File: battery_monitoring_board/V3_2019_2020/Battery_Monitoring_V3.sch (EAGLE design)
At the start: 82 parts, among them CON1 MOLEX_5566-2, CON2 SM03B-GHS-TB, CON3 SM03B-GHS-TB, J1 MKDS_5/2-6,352, J2 MKDS_5/2-6,352, J3 MKDS_5/2-6,352, J4 MKDS_5/2-6,352, J5 MKDS_5/2-6,352, J6 MKDS_5/2-6,352, J7 MKDS_5/2-6,352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

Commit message: battery_monitoring_board: moved V3 out into new folder
BOM and other exports still need to be finished
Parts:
- added D4: BZT52C10, Moira:BZT52C10
- added J10, J11: MKDS_5/2-6,352, Moira:MKDS_5/2-6,352
- added Q15: PSMN1R5-30BLE, Moira:PSMN1R5-30BLE
- added Q16: TCLD1000CT, Moira:TCLD1000CT
- added Q8: SI7145DP, Si7145DP:SI7145DP
- added R31, R32: 10k, adafruit:R-US_M1206
- added R33: 1k, adafruit:R-US_M1206
- added R34: 1k, adafruit:R-US_R0805
- added R35: 0.001Ohm, Moira:HCS3920FT1L00
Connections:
- new net BATT5GND: D4.A, J10.KL, Q15.S, R31.1, R32.1
- new net BATTERY5_IN: J10.KL1, Q8.S
- new net BATTERY_5: Q16.C2, Q8.D, R35.2, U1.IN+3
- new net MG4: D4.C, Q15.G, R32.2, R33.1
- new net MOTOR4: J11.KL, R35.1, U1.IN-3
- new net N$10: Q8.G, R31.2
- new net N$15: Q16.E, R33.2
- new net N$16: Q16.A, R34.2
- net +5V: now also R34.1
- net GND: now also J11.KL1, Q15.D
- net MOTOR2: no longer U1.IN-3
- net N$4: now also Q16.C1
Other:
- note added: "motor Gnd"
- moved on the sheet: CON1G$1, CON1G$2, JP1, JP2, JP3

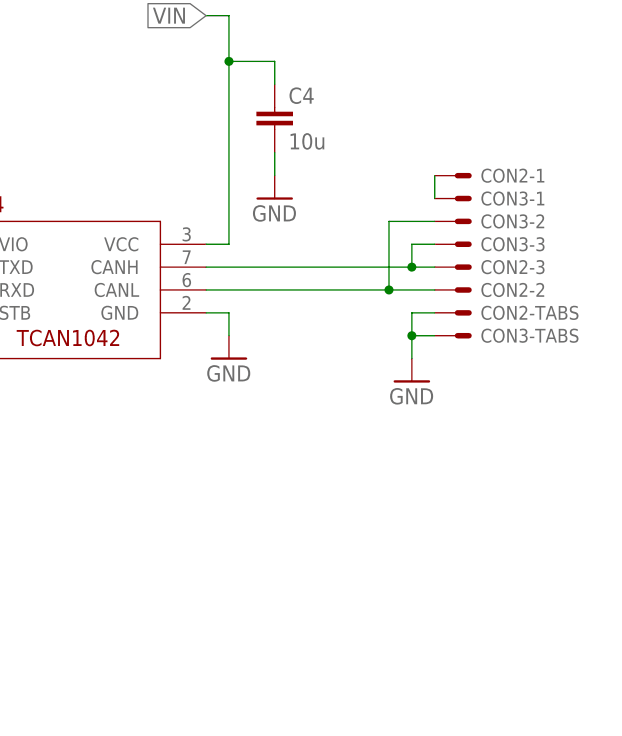
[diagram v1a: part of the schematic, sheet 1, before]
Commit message: battery_monitoring: replaced CAN with 4-pin header + better dimensions
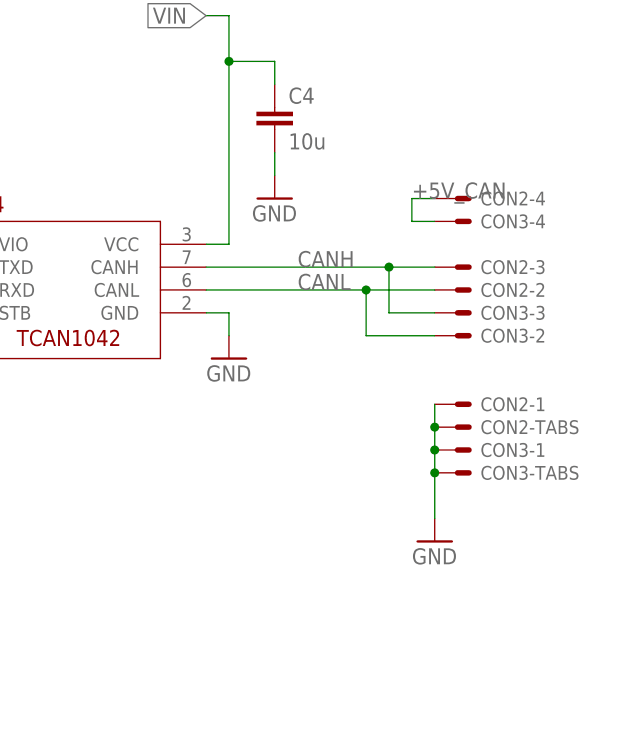
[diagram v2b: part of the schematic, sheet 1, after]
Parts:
- CON2, CON3: value SM03B-GHS-TB -> SM04B-GHS-TB; device ARVP:SM03B-GHS-TB -> ARVP:SM04B-GHS-TB
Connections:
- net CANH1 renamed CANH
- net CANL1 renamed CANL
- removed net CANSH1: CON2-1.S, CON3-1.S
- new net +5V_CAN: CON2-4.S, CON3-4.S
- net GND: now also CON2-1.S, CON3-1.S
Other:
- moved on the sheet: CON2-1, CON2-TABS, CON3-1, CON3-2, CON3-3, CON3-TABS
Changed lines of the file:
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@@
 <?xml version="1.0" encoding="utf-8"?>
 <!DOCTYPE eagle SYSTEM "eagle.dtd">
-<eagle version="9.5.1">
+<eagle version="9.6.1">
 <drawing>
 <settings>
@@
 <part name="R18" library="rcl" library_urn="urn:adsk.eagle:library:334" deviceset="R-US_" device="R0805" package3d_urn="urn:adsk.eagle:package:23553/2" value="1k"/>
 <part name="GND17" library="supply1" library_urn="urn:adsk.eagle:library:371" deviceset="GND" device=""/>
-<part name="CON2" library="ARVP" deviceset="SM03B-GHS-TB" device=""/>
-<part name="GND20" library="supply1" library_urn="urn:adsk.eagle:library:371" deviceset="GND" device=""/>
-<part name="CON3" library="ARVP" deviceset="SM03B-GHS-TB" device=""/>
 <part name="GND7" library="supply1" deviceset="GND" device=""/>
 <part name="JP1" library="pinhead" library_urn="urn:adsk.eagle:library:325" deviceset="PINHD-1X2" device="" package3d_urn="urn:adsk.eagle:package:22435/2"/>
@@
 <part name="J11" library="Moira" deviceset="MKDS_5/2-6,35" device="2"/>
 <part name="R35" library="Moira" deviceset="HCS3920" device="FT1L00" value="0.001Ohm"/>
+<part name="CON2" library="ARVP" deviceset="SM04B-GHS-TB" device=""/>
+<part name="CON3" library="ARVP" deviceset="SM04B-GHS-TB" device=""/>
+<part name="GND20" library="supply1" library_urn="urn:adsk.eagle:library:371" deviceset="GND" device=""/>
 </parts>
 <sheets>
@@
 <attribute name="VALUE" x="152.4" y="-104.14" size="1.778" layer="96"/>
 </instance>
-<instance part="CON2" gate="-1" x="213.36" y="-58.42" smashed="yes">
-<attribute name="NAME" x="218.44" y="-59.182" size="1.524" layer="95"/>
-</instance>
-<instance part="CON2" gate="-2" x="213.36" y="-71.12" smashed="yes">
-<attribute name="NAME" x="218.44" y="-71.882" size="1.524" layer="95"/>
-</instance>
-<instance part="CON2" gate="-3" x="213.36" y="-68.58" smashed="yes">
-<attribute name="NAME" x="218.44" y="-69.342" size="1.524" layer="95"/>
-</instance>
-<instance part="CON2" gate="-TABS" x="213.36" y="-73.66" smashed="yes">
-<attribute name="NAME" x="218.44" y="-74.422" size="1.524" layer="95"/>
-</instance>
-<instance part="GND20" gate="1" x="210.82" y="-81.28" smashed="yes">
-<attribute name="VALUE" x="208.28" y="-83.82" size="1.778" layer="96"/>
-</instance>
-<instance part="CON3" gate="-1" x="213.36" y="-60.96" smashed="yes">
-<attribute name="NAME" x="218.44" y="-61.722" size="1.524" layer="95"/>
-</instance>
-<instance part="CON3" gate="-2" x="213.36" y="-63.5" smashed="yes">
-<attribute name="NAME" x="218.44" y="-64.262" size="1.524" layer="95"/>
-</instance>
-<instance part="CON3" gate="-3" x="213.36" y="-66.04" smashed="yes">
-<attribute name="NAME" x="218.44" y="-66.802" size="1.524" layer="95"/>
-</instance>
-<instance part="CON3" gate="-TABS" x="213.36" y="-76.2" smashed="yes">
-<attribute name="NAME" x="218.44" y="-76.962" size="1.524" layer="95"/>
-</instance>
 <instance part="GND7" gate="1" x="-35.56" y="106.68" smashed="yes" rot="R270">
 <attribute name="VALUE" x="-38.1" y="109.22" size="1.778" layer="96" rot="R270"/>
@@
 <attribute name="NAME" x="34.5186" y="69.85" size="1.778" layer="95" rot="R270"/>
 <attribute name="VALUE" x="37.338" y="72.39" size="1.778" layer="96" rot="R270"/>
+</instance>
+<instance part="CON2" gate="-1" x="213.36" y="-83.82" smashed="yes">
+<attribute name="NAME" x="218.44" y="-84.582" size="1.524" layer="95"/>
+</instance>
+<instance part="CON2" gate="-2" x="213.36" y="-71.12" smashed="yes">
+<attribute name="NAME" x="218.44" y="-71.882" size="1.524" layer="95"/>
+</instance>
+<instance part="CON2" gate="-3" x="213.36" y="-68.58" smashed="yes">
+<attribute name="NAME" x="218.44" y="-69.342" size="1.524" layer="95"/>
+</instance>
+<instance part="CON2" gate="-TABS" x="213.36" y="-86.36" smashed="yes">
+<attribute name="NAME" x="218.44" y="-87.122" size="1.524" layer="95"/>
+</instance>
+<instance part="CON2" gate="-4" x="213.36" y="-60.96" smashed="yes">
+<attribute name="NAME" x="218.44" y="-61.722" size="1.524" layer="95"/>
+</instance>
+<instance part="CON3" gate="-1" x="213.36" y="-88.9" smashed="yes">
+<attribute name="NAME" x="218.44" y="-89.662" size="1.524" layer="95"/>
+</instance>
+<instance part="CON3" gate="-2" x="213.36" y="-76.2" smashed="yes">
+<attribute name="NAME" x="218.44" y="-76.962" size="1.524" layer="95"/>
+</instance>
+<instance part="CON3" gate="-3" x="213.36" y="-73.66" smashed="yes">
+<attribute name="NAME" x="218.44" y="-74.422" size="1.524" layer="95"/>
+</instance>
+<instance part="CON3" gate="-TABS" x="213.36" y="-91.44" smashed="yes">
+<attribute name="NAME" x="218.44" y="-92.202" size="1.524" layer="95"/>
+</instance>
+<instance part="CON3" gate="-4" x="213.36" y="-63.5" smashed="yes">
+<attribute name="NAME" x="218.44" y="-64.262" size="1.524" layer="95"/>
+</instance>
+<instance part="GND20" gate="1" x="213.36" y="-99.06" smashed="yes">
+<attribute name="VALUE" x="210.82" y="-101.6" size="1.778" layer="96"/>
 </instance>
 </instances>
@@
 </segment>
 <segment>
-<pinref part="GND20" gate="1" pin="GND"/>
-<wire x1="210.82" y1="-78.74" x2="210.82" y2="-76.2" width="0.1524" layer="91"/>
-<pinref part="CON2" gate="-TABS" pin="S"/>
-<wire x1="210.82" y1="-76.2" x2="210.82" y2="-73.66" width="0.1524" layer="91"/>
-<wire x1="210.82" y1="-73.66" x2="213.36" y2="-73.66" width="0.1524" layer="91"/>
-<pinref part="CON3" gate="-TABS" pin="S"/>
-<wire x1="210.82" y1="-76.2" x2="213.36" y2="-76.2" width="0.1524" layer="91"/>
-<junction x="210.82" y="-76.2"/>
-</segment>
-<segment>
 <pinref part="J8" gate="G$1" pin="KL1"/>
 <wire x1="-33.02" y1="106.68" x2="-25.4" y2="106.68" width="0.1524" layer="91"/>
@@
 <wire x1="-25.4" y1="-71.12" x2="-139.7" y2="-71.12" width="0.1524" layer="91"/>
 <junction x="-139.7" y="-71.12"/>
+</segment>
+<segment>
+<pinref part="CON2" gate="-1" pin="S"/>
+<pinref part="CON2" gate="-TABS" pin="S"/>
+<wire x1="213.36" y1="-83.82" x2="213.36" y2="-86.36" width="0.1524" layer="91"/>
+<pinref part="CON3" gate="-1" pin="S"/>
+<wire x1="213.36" y1="-86.36" x2="213.36" y2="-88.9" width="0.1524" layer="91"/>
+<junction x="213.36" y="-86.36"/>
+<pinref part="CON3" gate="-TABS" pin="S"/>
+<wire x1="213.36" y1="-88.9" x2="213.36" y2="-91.44" width="0.1524" layer="91"/>
+<junction x="213.36" y="-88.9"/>
+<junction x="213.36" y="-91.44"/>
+<wire x1="213.36" y1="-91.44" x2="213.36" y2="-96.52" width="0.1524" layer="91"/>
+<pinref part="GND20" gate="1" pin="GND"/>
 </segment>
 </net>
@@
 </segment>
 </net>
-<net name="CANH1" class="0">
+<net name="CANH" class="0">
 <segment>
 <pinref part="U4" gate="G$1" pin="CANH"/>
+<wire x1="187.96" y1="-68.58" x2="208.28" y2="-68.58" width="0.1524" layer="91"/>
 <pinref part="CON2" gate="-3" pin="S"/>
-<wire x1="187.96" y1="-68.58" x2="210.82" y2="-68.58" width="0.1524" layer="91"/>
+<wire x1="208.28" y1="-68.58" x2="213.36" y2="-68.58" width="0.1524" layer="91"/>
+<wire x1="208.28" y1="-68.58" x2="208.28" y2="-73.66" width="0.1524" layer="91"/>
+<junction x="208.28" y="-68.58"/>
 <pinref part="CON3" gate="-3" pin="S"/>
-<wire x1="210.82" y1="-68.58" x2="213.36" y2="-68.58" width="0.1524" layer="91"/>
-<wire x1="213.36" y1="-66.04" x2="210.82" y2="-66.04" width="0.1524" layer="91"/>
-<wire x1="210.82" y1="-66.04" x2="210.82" y2="-68.58" width="0.1524" layer="91"/>
-<junction x="210.82" y="-68.58"/>
-</segment>
-</net>
-<net name="CANL1" class="0">
+<wire x1="208.28" y1="-73.66" x2="213.36" y2="-73.66" width="0.1524" layer="91"/>
+<label x="198.12" y="-68.58" size="1.778" layer="95"/>
+</segment>
+</net>
+<net name="CANL" class="0">
 <segment>
 <pinref part="U4" gate="G$1" pin="CANL"/>
+<wire x1="187.96" y1="-71.12" x2="205.74" y2="-71.12" width="0.1524" layer="91"/>
 <pinref part="CON2" gate="-2" pin="S"/>
-<wire x1="187.96" y1="-71.12" x2="208.28" y2="-71.12" width="0.1524" layer="91"/>
+<wire x1="205.74" y1="-71.12" x2="213.36" y2="-71.12" width="0.1524" layer="91"/>
+<wire x1="205.74" y1="-71.12" x2="205.74" y2="-76.2" width="0.1524" layer="91"/>
+<junction x="205.74" y="-71.12"/>
 <pinref part="CON3" gate="-2" pin="S"/>
-<wire x1="208.28" y1="-71.12" x2="213.36" y2="-71.12" width="0.1524" layer="91"/>
-<wire x1="213.36" y1="-63.5" x2="208.28" y2="-63.5" width="0.1524" layer="91"/>
-<wire x1="208.28" y1="-63.5" x2="208.28" y2="-71.12" width="0.1524" layer="91"/>
-<junction x="208.28" y="-71.12"/>
-</segment>
-</net>
-<net name="CANSH1" class="0">
-<segment>
-<pinref part="CON2" gate="-1" pin="S"/>
-<pinref part="CON3" gate="-1" pin="S"/>
-<wire x1="213.36" y1="-58.42" x2="213.36" y2="-60.96" width="0.1524" layer="91"/>
+<wire x1="205.74" y1="-76.2" x2="213.36" y2="-76.2" width="0.1524" layer="91"/>
+<label x="198.12" y="-71.12" size="1.778" layer="95"/>
 </segment>
 </net>
@@
 </segment>
 </net>
+<net name="+5V_CAN" class="0">
+<segment>
+<pinref part="CON2" gate="-4" pin="S"/>
+<wire x1="213.36" y1="-60.96" x2="210.82" y2="-60.96" width="0.1524" layer="91"/>
+<wire x1="210.82" y1="-60.96" x2="210.82" y2="-63.5" width="0.1524" layer="91"/>
+<pinref part="CON3" gate="-4" pin="S"/>
+<wire x1="210.82" y1="-63.5" x2="213.36" y2="-63.5" width="0.1524" layer="91"/>
+<label x="210.82" y="-60.96" size="1.778" layer="95"/>
+</segment>
+</net>
